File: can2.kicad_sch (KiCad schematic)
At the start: 7 parts, among them U1 TJA1042T-3

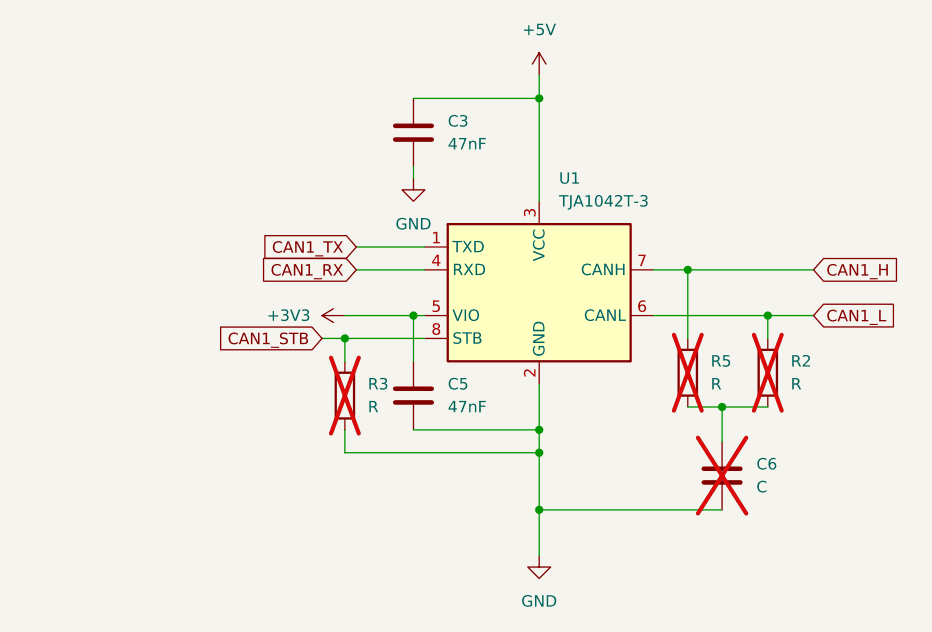
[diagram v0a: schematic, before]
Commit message: add CAN2 and CAN3
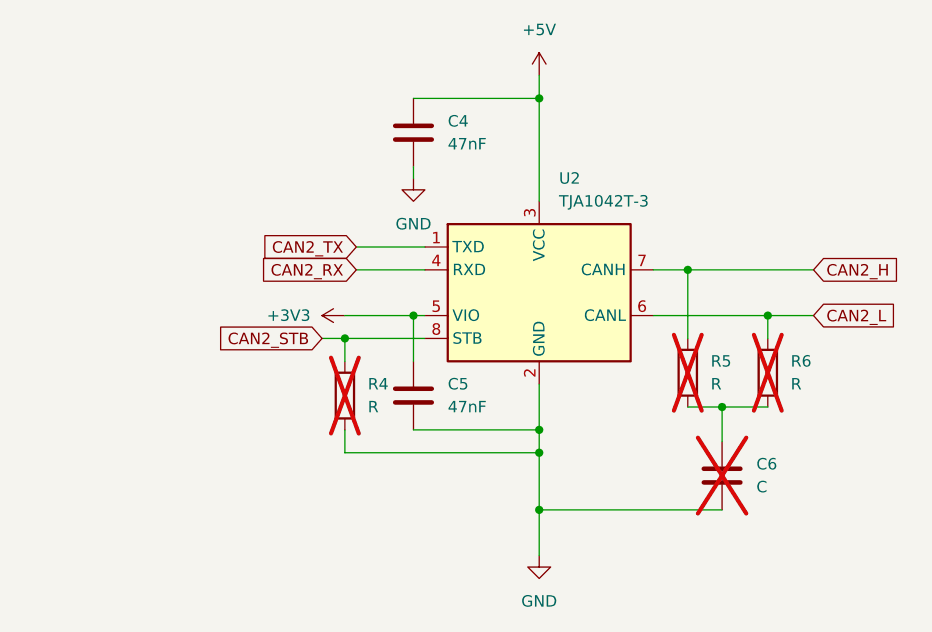
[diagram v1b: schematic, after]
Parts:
- renumbered C3 to C4, R3 to R4, R2 to R6, U1 to U2
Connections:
- net CAN1_H renamed CAN2_H
- net CAN1_L renamed CAN2_L
- net CAN1_RX renamed CAN2_RX
- net CAN1_STB renamed CAN2_STB
- net CAN1_TX renamed CAN2_TX
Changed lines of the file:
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@@
 		)
 	)
-	(global_label "CAN1_H"
+	(global_label "CAN2_H"
 		(shape input)
 		(at 156.21 80.01 0)
@@
 		)
 	)
-	(global_label "CAN1_L"
+	(global_label "CAN2_L"
 		(shape input)
 		(at 156.21 85.09 0)
@@
 		)
 	)
-	(global_label "CAN1_TX"
+	(global_label "CAN2_TX"
 		(shape input)
 		(at 105.41 77.47 180)
@@
 		)
 	)
-	(global_label "CAN1_STB"
+	(global_label "CAN2_STB"
 		(shape input)
 		(at 101.6 87.63 180)
@@
 		)
 	)
-	(global_label "CAN1_RX"
+	(global_label "CAN2_RX"
 		(shape input)
 		(at 105.41 80.01 180)
@@
 		(dnp no)
 		(fields_autoplaced yes)
-		(property "Reference" "#PWR015"
+		(property "Reference" "#PWR017"
 			(at 107.95 85.09 0)
 			(effects
@@
 		(instances
 			(project "sample"
-				(path "/b24c09df-2e49-4fc3-a45d-ba0b1ff2d257/a1e1f3d2-08a6-4ef9-b40d-891f90ca343c"
-					(reference "#PWR015")
+				(path "/b24c09df-2e49-4fc3-a45d-ba0b1ff2d257/ecc88370-915d-48f9-8e29-e68ead91d11e"
+					(reference "#PWR017")
+					(unit 1)
+				)
+				(path "/b24c09df-2e49-4fc3-a45d-ba0b1ff2d257/f47ed58f-27f7-4b09-9f1c-00de47ea5151"
+					(reference "#PWR016")
 					(unit 1)
 				)
@@
 		(dnp no)
 		(fields_autoplaced yes)
-		(property "Reference" "#PWR013"
+		(property "Reference" "#PWR020"
 			(at 125.73 118.11 0)
 			(effects
@@
 		(instances
 			(project "sample"
-				(path "/b24c09df-2e49-4fc3-a45d-ba0b1ff2d257/a1e1f3d2-08a6-4ef9-b40d-891f90ca343c"
-					(reference "#PWR013")
+				(path "/b24c09df-2e49-4fc3-a45d-ba0b1ff2d257/ecc88370-915d-48f9-8e29-e68ead91d11e"
+					(reference "#PWR020")
+					(unit 1)
+				)
+				(path "/b24c09df-2e49-4fc3-a45d-ba0b1ff2d257/f47ed58f-27f7-4b09-9f1c-00de47ea5151"
+					(reference "#PWR023")
 					(unit 1)
 				)
@@
 		(dnp yes)
 		(fields_autoplaced yes)
-		(property "Reference" "R2"
+		(property "Reference" "R6"
 			(at 153.67 90.1699 0)
 			(effects
@@
 		(instances
 			(project "sample"
-				(path "/b24c09df-2e49-4fc3-a45d-ba0b1ff2d257/a1e1f3d2-08a6-4ef9-b40d-891f90ca343c"
-					(reference "R2")
+				(path "/b24c09df-2e49-4fc3-a45d-ba0b1ff2d257/ecc88370-915d-48f9-8e29-e68ead91d11e"
+					(reference "R6")
+					(unit 1)
+				)
+				(path "/b24c09df-2e49-4fc3-a45d-ba0b1ff2d257/f47ed58f-27f7-4b09-9f1c-00de47ea5151"
+					(reference "R8")
 					(unit 1)
 				)
@@
 		(pin "1"
 		)
+		(instances
+			(project "sample"
+				(path "/b24c09df-2e49-4fc3-a45d-ba0b1ff2d257/ecc88370-915d-48f9-8e29-e68ead91d11e"
+					(reference "C5")
+					(unit 1)
+				)
+				(path "/b24c09df-2e49-4fc3-a45d-ba0b1ff2d257/f47ed58f-27f7-4b09-9f1c-00de47ea5151"
+					(reference "C2")
+					(unit 1)
+				)
+			)
+		)
 	)
 	(symbol
@@
 		(dnp no)
 		(fields_autoplaced yes)
-		(property "Reference" "U1"
+		(property "Reference" "U2"
 			(at 127.9241 69.85 0)
 			(effects
@@
 		(instances
 			(project "sample"
-				(path "/b24c09df-2e49-4fc3-a45d-ba0b1ff2d257/a1e1f3d2-08a6-4ef9-b40d-891f90ca343c"
-					(reference "U1")
+				(path "/b24c09df-2e49-4fc3-a45d-ba0b1ff2d257/ecc88370-915d-48f9-8e29-e68ead91d11e"
+					(reference "U2")
+					(unit 1)
+				)
+				(path "/b24c09df-2e49-4fc3-a45d-ba0b1ff2d257/f47ed58f-27f7-4b09-9f1c-00de47ea5151"
+					(reference "U3")
 					(unit 1)
 				)
@@
 		(dnp no)
 		(fields_autoplaced yes)
-		(property "Reference" "#PWR014"
+		(property "Reference" "#PWR019"
 			(at 125.73 62.23 0)
 			(effects
@@
 		(instances
 			(project "sample"
-				(path "/b24c09df-2e49-4fc3-a45d-ba0b1ff2d257/a1e1f3d2-08a6-4ef9-b40d-891f90ca343c"
-					(reference "#PWR014")
+				(path "/b24c09df-2e49-4fc3-a45d-ba0b1ff2d257/ecc88370-915d-48f9-8e29-e68ead91d11e"
+					(reference "#PWR019")
+					(unit 1)
+				)
+				(path "/b24c09df-2e49-4fc3-a45d-ba0b1ff2d257/f47ed58f-27f7-4b09-9f1c-00de47ea5151"
+					(reference "#PWR022")
 					(unit 1)
 				)
@@
 		(pin "1"
 		)
+		(instances
+			(project "sample"
+				(path "/b24c09df-2e49-4fc3-a45d-ba0b1ff2d257/ecc88370-915d-48f9-8e29-e68ead91d11e"
+					(reference "R5")
+					(unit 1)
+				)
+				(path "/b24c09df-2e49-4fc3-a45d-ba0b1ff2d257/f47ed58f-27f7-4b09-9f1c-00de47ea5151"
+					(reference "R7")
+					(unit 1)
+				)
+			)
+		)
 	)
 	(symbol
@@
 		(dnp yes)
 		(fields_autoplaced yes)
-		(property "Reference" "R3"
+		(property "Reference" "R4"
 			(at 106.68 92.7099 0)
 			(effects
@@
 		(instances
 			(project "sample"
-				(path "/b24c09df-2e49-4fc3-a45d-ba0b1ff2d257/a1e1f3d2-08a6-4ef9-b40d-891f90ca343c"
-					(reference "R3")
+				(path "/b24c09df-2e49-4fc3-a45d-ba0b1ff2d257/ecc88370-915d-48f9-8e29-e68ead91d11e"
+					(reference "R4")
+					(unit 1)
+				)
+				(path "/b24c09df-2e49-4fc3-a45d-ba0b1ff2d257/f47ed58f-27f7-4b09-9f1c-00de47ea5151"
+					(reference "R1")
 					(unit 1)
 				)
@@
 		(pin "1"
 		)
+		(instances
+			(project "sample"
+				(path "/b24c09df-2e49-4fc3-a45d-ba0b1ff2d257/ecc88370-915d-48f9-8e29-e68ead91d11e"
+					(reference "#PWR018")
+					(unit 1)
+				)
+				(path "/b24c09df-2e49-4fc3-a45d-ba0b1ff2d257/f47ed58f-27f7-4b09-9f1c-00de47ea5151"
+					(reference "#PWR021")
+					(unit 1)
+				)
+			)
+		)
 	)
 	(symbol
@@
 		(dnp no)
 		(fields_autoplaced yes)
-		(property "Reference" "C3"
+		(property "Reference" "C4"
 			(at 115.57 63.4999 0)
 			(effects
@@
 		(instances
 			(project "sample"
-				(path "/b24c09df-2e49-4fc3-a45d-ba0b1ff2d257/a1e1f3d2-08a6-4ef9-b40d-891f90ca343c"
-					(reference "C3")
+				(path "/b24c09df-2e49-4fc3-a45d-ba0b1ff2d257/ecc88370-915d-48f9-8e29-e68ead91d11e"
+					(reference "C4")
+					(unit 1)
+				)
+				(path "/b24c09df-2e49-4fc3-a45d-ba0b1ff2d257/f47ed58f-27f7-4b09-9f1c-00de47ea5151"
+					(reference "C1")
 					(unit 1)
 				)
@@
 		(pin "1"
 		)
-	)
+		(instances
+			(project "sample"
+				(path "/b24c09df-2e49-4fc3-a45d-ba0b1ff2d257/ecc88370-915d-48f9-8e29-e68ead91d11e"
+					(reference "C6")
+					(unit 1)
+				)
+				(path "/b24c09df-2e49-4fc3-a45d-ba0b1ff2d257/f47ed58f-27f7-4b09-9f1c-00de47ea5151"
+					(reference "C7")
+					(unit 1)
+				)
+			)
+		)
+	)

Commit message: fix double numbers
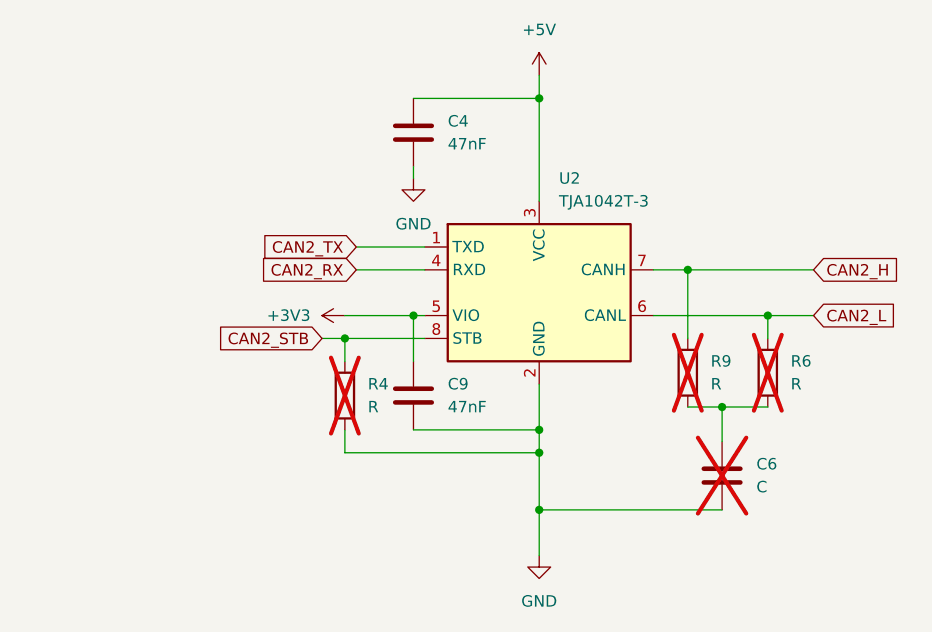
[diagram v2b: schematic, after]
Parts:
- removed C5: 47nF, Capacitor_SMD:C_1206_3216Metric_Pad1.33x1.80mm_HandSolder, symbol Device:C
- removed R5: R, Resistor_SMD:R_1206_3216Metric_Pad1.30x1.75mm_HandSolder, symbol Device:R
- added C9: 47nF, Capacitor_SMD:C_1206_3216Metric_Pad1.33x1.80mm_HandSolder, symbol Device:C
- added R9: R, Resistor_SMD:R_1206_3216Metric_Pad1.30x1.75mm_HandSolder, symbol Device:R
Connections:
- net +3V3: now also C9.1
- net CAN2_H: now also R9.1
- net GND: now also C9.2
- net at C6.1, R6.2: now also R9.2

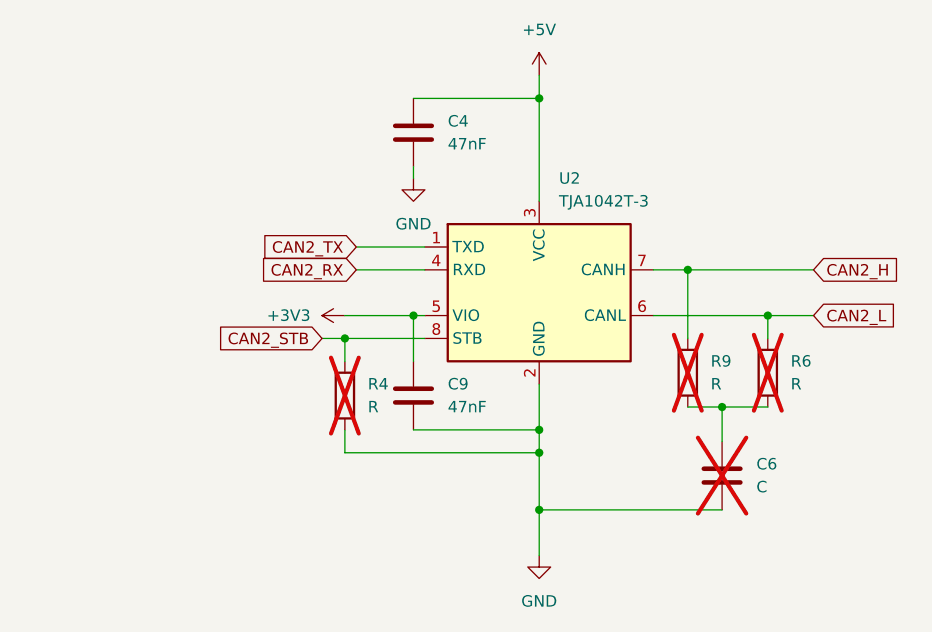
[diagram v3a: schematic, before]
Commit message: add CAN STB pins
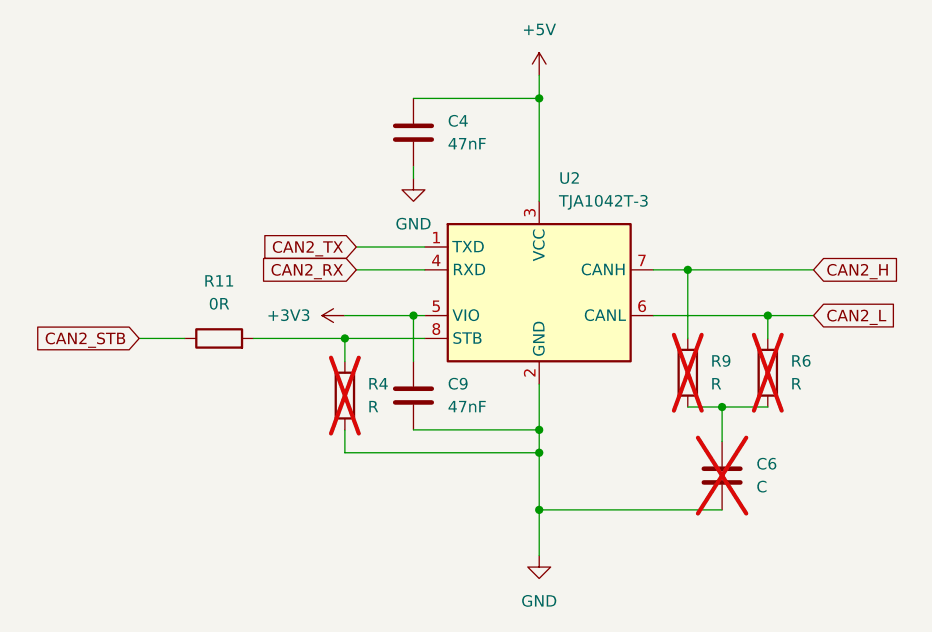
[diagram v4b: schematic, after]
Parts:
- added R11: 0R, Resistor_SMD:R_1206_3216Metric_Pad1.30x1.75mm_HandSolder, symbol Device:R
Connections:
- net CAN2_STB: now also R11.1; no longer R4.1, U2.8 (STB)
- new net: R11.2, R4.1, U2.8 (STB)
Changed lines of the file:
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@@
+	(wire
+		(pts
+			(xy 81.28 87.63) (xy 86.36 87.63)
+		)
+		(stroke
+			(width 0)
+			(type default)
+		)
+	)
 	(wire
 		(pts
@@
 	(wire
 		(pts
+			(xy 93.98 87.63) (xy 104.14 87.63)
+		)
+		(stroke
+			(width 0)
+			(type default)
+		)
+	)
+	(wire
+		(pts
 			(xy 146.05 95.25) (xy 146.05 99.06)
 		)
@@
 		(pts
 			(xy 125.73 60.96) (xy 125.73 72.39)
-		)
-		(stroke
-			(width 0)
-			(type default)
-		)
-	)
-	(wire
-		(pts
-			(xy 101.6 87.63) (xy 104.14 87.63)
 		)
 		(stroke
@@
 	(global_label "CAN2_STB"
 		(shape input)
-		(at 101.6 87.63 180)
+		(at 81.28 87.63 180)
 		(fields_autoplaced yes)
 		(effects
@@
 		)
 		(property "Intersheetrefs" "${INTERSHEET_REFS}"
-			(at 89.3015 87.63 0)
+			(at 68.9815 87.63 0)
 			(effects
 				(font
@@
 					(unit 1)
 				)
+			)
+		)
+	)
+	(symbol
+		(lib_id "Device:R")
+		(at 90.17 87.63 90)
+		(unit 1)
+		(exclude_from_sim no)
+		(in_bom yes)
+		(on_board yes)
+		(dnp no)
+		(fields_autoplaced yes)
+		(property "Reference" "R11"
+			(at 90.17 81.28 90)
+			(effects
+				(font
+					(size 1.27 1.27)
+				)
+			)
+		)
+		(property "Value" "0R"
+			(at 90.17 83.82 90)
+			(effects
+				(font
+					(size 1.27 1.27)
+				)
+			)
+		)
+		(property "Footprint" "Resistor_SMD:R_1206_3216Metric_Pad1.30x1.75mm_HandSolder"
+			(at 90.17 89.408 90)
+			(effects
+				(font
+					(size 1.27 1.27)
+				)
+				(hide yes)
+			)
+		)
+		(property "Datasheet" "~"
+			(at 90.17 87.63 0)
+			(effects
+				(font
+					(size 1.27 1.27)
+				)
+				(hide yes)
+			)
+		)
+		(property "Description" "Resistor"
+			(at 90.17 87.63 0)
+			(effects
+				(font
+					(size 1.27 1.27)
+				)
+				(hide yes)
+			)
+		)
+		(pin "2"
+		)
+		(pin "1"
+		)
+		(instances
+			(project "sample"
+				(path "/b24c09df-2e49-4fc3-a45d-ba0b1ff2d257/ecc88370-915d-48f9-8e29-e68ead91d11e"
+					(reference "R11")
+					(unit 1)
+				)
